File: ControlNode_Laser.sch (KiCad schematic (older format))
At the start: 2 parts

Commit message: Split accels off to separate sheet.
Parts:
- removed P?: CONN_01X07, symbol CONN_01X07
- added C? (x4): 100n, symbol C
- added P?: CONN_01X08_2MNT, symbol CONN_01X08_2MNT
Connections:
- net labels added: LRF_ANALOG_OUT, LRF_RX_232, LRF_TRIGGER_IN, LRF_TRIGGER_OUT, LRF_TX_232
- net labels removed: LRD_Analog_Output, LRD_Trigger_Input, LRF_Rx, LRF_Trigger_Output, LRF_Tx, P1, P2
- wire segments 8 -> 22
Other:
- note added: "Original Author: SafetyLok"
- note added: "rLoop - Control Node"
- note removed: "Test Point x2\n"
- moved on the sheet: U?
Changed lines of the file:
@@
 $Descr A3 16535 11693
 encoding utf-8
-Sheet 2 2
+Sheet 2 3
 Title "Laser Interface"
 Date ""
@@
 Comment4 ""
 $EndDescr
-$Comp
-L CONN_01X07 P?
-U 1 1 5753FF72
-P 4750 3400
-F 0 "P?" H 4750 3800 50  0000 C CNN
-F 1 "CONN_01X07" V 4850 3400 50  0000 C CNN
-F 2 "" H 4750 3400 50  0000 C CNN
-F 3 "" H 4750 3400 50  0000 C CNN
-	1    4750 3400
-	-1   0    0    1
-$EndComp
-Text Notes 4350 2950 0    60   ~ 0
+Text Notes 11700 5200 1    60   ~ 0
 Laser Rangefinder CM3-30\nRS-232
 $Comp
 L +24V #PWR?
 U 1 1 5753FF7A
-P 5350 4000
-F 0 "#PWR?" H 5350 3850 50  0001 C CNN
-F 1 "+24V" H 5350 4140 50  0000 C CNN
-F 2 "" H 5350 4000 50  0000 C CNN
-F 3 "" H 5350 4000 50  0000 C CNN
-	1    5350 4000
+P 10850 4300
+F 0 "#PWR?" H 10850 4150 50  0001 C CNN
+F 1 "+24V" H 10850 4440 50  0000 C CNN
+F 2 "" H 10850 4300 50  0000 C CNN
+F 3 "" H 10850 4300 50  0000 C CNN
+	1    10850 4300
 	1    0    0    -1
 $EndComp
@@
 L GND #PWR?
 U 1 1 5753FF80
-P 5600 3750
-F 0 "#PWR?" H 5600 3500 50  0001 C CNN
-F 1 "GND" H 5600 3600 50  0000 C CNN
-F 2 "" H 5600 3750 50  0000 C CNN
-F 3 "" H 5600 3750 50  0000 C CNN
-	1    5600 3750
+P 10850 4450
+F 0 "#PWR?" H 10850 4200 50  0001 C CNN
+F 1 "GND" H 10850 4300 50  0000 C CNN
+F 2 "" H 10850 4450 50  0000 C CNN
+F 3 "" H 10850 4450 50  0000 C CNN
+	1    10850 4450
+	0    1    1    0
+$EndComp
+$Comp
+L MAX3232 U?
+U 1 1 575400BF
+P 6500 4250
+F 0 "U?" H 7500 4350 60  0000 C CNN
+F 1 "MAX3232" H 7300 2700 60  0000 C CNN
+F 2 "" H 6500 4250 60  0000 C CNN
+F 3 "" H 6500 4250 60  0000 C CNN
+	1    6500 4250
+	1    0    0    -1
+$EndComp
+Text HLabel 5300 5400 0    63   Output ~ 0
+LASER_RX
+Text HLabel 5300 5200 0    63   Input ~ 0
+LASER_TX
+$Comp
+L C C?
+U 1 1 5754B550
+P 5850 4450
+F 0 "C?" H 5875 4550 50  0000 L CNN
+F 1 "100n" H 5875 4350 50  0000 L CNN
+F 2 "" H 5888 4300 50  0000 C CNN
+F 3 "" H 5850 4450 50  0000 C CNN
+	1    5850 4450
+	0    1    1    0
+$EndComp
+$Comp
+L C C?
+U 1 1 5754A89B
+P 5850 4950
+F 0 "C?" H 5875 5050 50  0000 L CNN
+F 1 "100n" H 5875 4850 50  0000 L CNN
+F 2 "" H 5888 4800 50  0000 C CNN
+F 3 "" H 5850 4950 50  0000 C CNN
+	1    5850 4950
+	0    1    1    0
+$EndComp
+$Comp
+L C C?
+U 1 1 5754A977
+P 6650 3900
+F 0 "C?" H 6675 4000 50  0000 L CNN
+F 1 "100n" H 6675 3800 50  0000 L CNN
+F 2 "" H 6688 3750 50  0000 C CNN
+F 3 "" H 6650 3900 50  0000 C CNN
+	1    6650 3900
+	1    0    0    -1
+$EndComp
+$Comp
+L C C?
+U 1 1 5754AA53
+P 6650 6250
+F 0 "C?" H 6675 6350 50  0000 L CNN
+F 1 "100n" H 6675 6150 50  0000 L CNN
+F 2 "" H 6688 6100 50  0000 C CNN
+F 3 "" H 6650 6250 50  0000 C CNN
+	1    6650 6250
 	1    0    0    -1
 $EndComp
 Wire Wire Line
-	4950 3700 4950 4000
+	6000 4450 6300 4450
 Wire Wire Line
-	4950 4000 5350 4000
+	6300 4650 5650 4650
 Wire Wire Line
-	4950 3600 5600 3600
+	5650 4650 5650 4450
 Wire Wire Line
-	5600 3600 5600 3750
+	5650 4450 5700 4450
 Wire Wire Line
-	4950 3500 5600 3500
+	6300 4950 6000 4950
 Wire Wire Line
-	4950 3400 5600 3400
+	6300 4750 5650 4750
 Wire Wire Line
-	4950 3300 6100 3300
+	5650 4750 5650 4950
 Wire Wire Line
-	4950 3200 6100 3200
-Text Label 5250 3500 0    60   ~ 0
-LRF_Tx
-Text Label 5250 3400 0    60   ~ 0
-LRF_Rx
-Text Label 5050 3300 0    60   ~ 0
-LRF_Trigger_Output
-Text Label 5050 3200 0    60   ~ 0
-LRD_Analog_Output
-Text Label 5050 3100 0    60   ~ 0
-LRD_Trigger_Input
-Text Notes 6350 3250 0    60   ~ 0
-Test Point x2\n
-Connection ~ 5600 3200
-Connection ~ 5600 3300
-Text Label 6100 3200 0    60   ~ 0
-P1
-Text Label 6100 3300 0    60   ~ 0
-P2
+	5650 4950 5700 4950
+Wire Wire Line
+	5300 5200 6300 5200
+Wire Wire Line
+	6300 5400 5300 5400
 $Comp
-L MAX3232 U?
-U 1 1 575400BF
-P 8450 3600
-F 0 "U?" H 8550 4300 60  0000 C CNN
-F 1 "MAX3232" H 8550 3150 60  0000 C CNN
-F 2 "" H 8450 3600 60  0000 C CNN
-F 3 "" H 8450 3600 60  0000 C CNN
-	1    8450 3600
+L CONN_01X08_2MNT P?
+U 1 1 5754B07F
+P 11250 4700
+F 0 "P?" H 11250 5150 50  0000 C CNN
+F 1 "CONN_01X08_2MNT" V 11350 4700 50  0000 C CNN
+F 2 "" H 11250 4700 50  0000 C CNN
+F 3 "" H 11250 4700 50  0000 C CNN
+	1    11250 4700
 	1    0    0    -1
 $EndComp
-Text HLabel 11150 3150 0    63   Output ~ 0
-LASER_RX
-Text HLabel 11100 3300 0    63   Input ~ 0
-LASER_TX
+Wire Wire Line
+	11050 4450 10850 4450
+Wire Wire Line
+	11050 4350 10850 4350
+Wire Wire Line
+	10850 4350 10850 4300
+Wire Wire Line
+	7750 5200 8950 5200
+Wire Wire Line
+	8950 5200 8950 4550
+Wire Wire Line
+	8950 4550 11050 4550
+Wire Wire Line
+	7750 5400 9050 5400
+Wire Wire Line
+	9050 5400 9050 4650
+Wire Wire Line
+	9050 4650 11050 4650
+Text Label 9400 4550 0    60   ~ 0
+LRF_TX_232
+Text Label 9400 4650 0    60   ~ 0
+LRF_RX_232
+Wire Wire Line
+	11050 4750 10000 4750
+Wire Wire Line
+	11050 4850 10000 4850
+Wire Wire Line
+	11050 4950 10000 4950
+Text Label 10100 4750 0    60   ~ 0
+LRF_TRIGGER_OUT
+Text Label 10100 4850 0    60   ~ 0
+LRF_ANALOG_OUT
+Text Label 10100 4950 0    60   ~ 0
+LRF_TRIGGER_IN
+Text Notes 11900 10200 0    118  ~ 0
+rLoop - Control Node
+Text Notes 11900 10400 0    60   ~ 0
+Original Author: SafetyLok
 $EndSCHEMATC

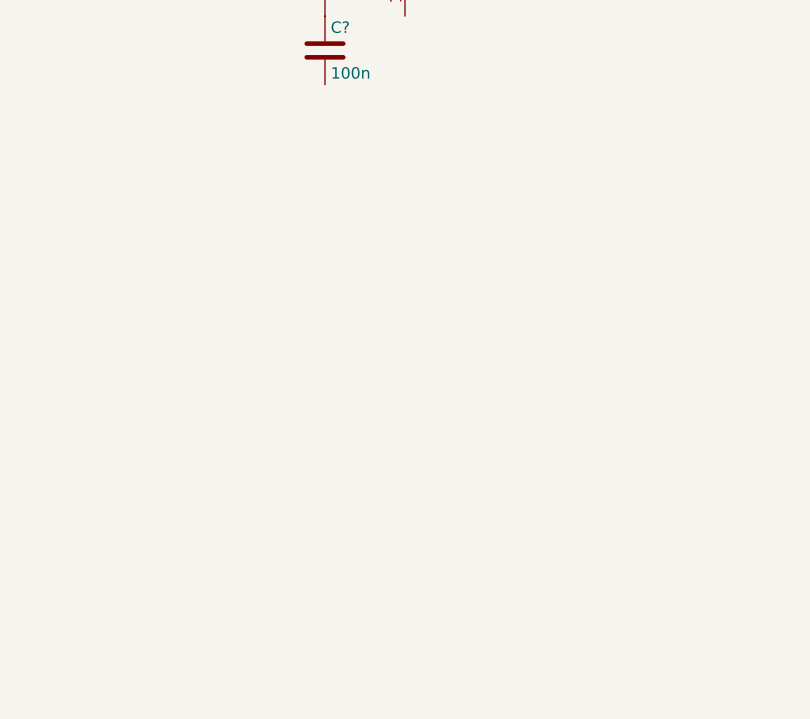
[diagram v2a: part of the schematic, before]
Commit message: Update height sensors.
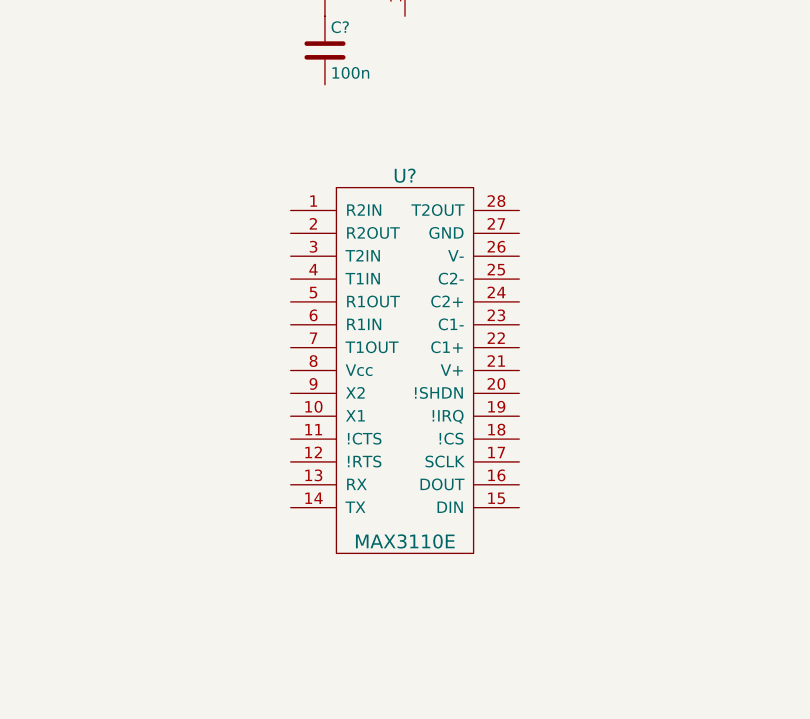
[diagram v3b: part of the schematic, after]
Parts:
- added U?: MAX3110E, symbol MAX3110E-RESCUE-Control_Board
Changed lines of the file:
@@
 Text Notes 11900 10400 0    60   ~ 0
 Original Author: SafetyLok
+$Comp
+L MAX3110E-RESCUE-Control_Board U?
+U 1 1 575676EE
+P 7350 7750
+AR Path="/575676EE" Ref="U?"  Part="1"
+AR Path="/5753FE7B/575676EE" Ref="U?"  Part="1"
+F 0 "U?" H 7000 8700 60  0000 C CNN
+F 1 "MAX3110E" H 7000 7100 60  0000 C CNN
+F 2 "" H 7350 7750 60  0000 C CNN
+F 3 "" H 7350 7750 60  0000 C CNN
+	1    7350 7750
+	1    0    0    -1
+$EndComp
 $EndSCHEMATC

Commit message: Release 1
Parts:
- removed C? (x4): 100n, symbol C
- removed P?: CONN_01X08_2MNT, symbol CONN_01X08_2MNT
- removed U?: MAX3232, symbol MAX3232
- removed U?: MAX3110E, symbol MAX3110E-RESCUE-Control_Board
- added C? (x5): C_100nF_50V, RLOOP_FOOTPRINTS:rLoop_C_0603, symbol C_100nF_50V
- added C? (x2): C_22pF_50V, RLOOP_FOOTPRINTS:rLoop_C_0603, symbol C_22pF_50V
- added P?: TE_640456-8, RLOOP_FOOTPRINTS:rLoop_TE640456-8, symbol TE_640456-8
- added U?: MAX3111EEWI+G36, RLOOP_FOOTPRINTS:rLoop_SOIC28, symbol MAX3111EEWI+G36
- added Y?: MP018S, RLOOP_FOOTPRINTS:rLoop_HC49, symbol MP018S
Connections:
- net labels added: +24V_A, +3V3_A, GNDD, LASER_NCS, LASER_NIRQ, LASER_SPI_MISO, LASER_SPI_MOSI, LASER_SPI_SCK
- net labels removed: +24V, GND, LASER_RX, LASER_TX
- wire segments 22 -> 27
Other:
- note added: "Notes:\n1. All Vreg capacitors are OPTIONAL."

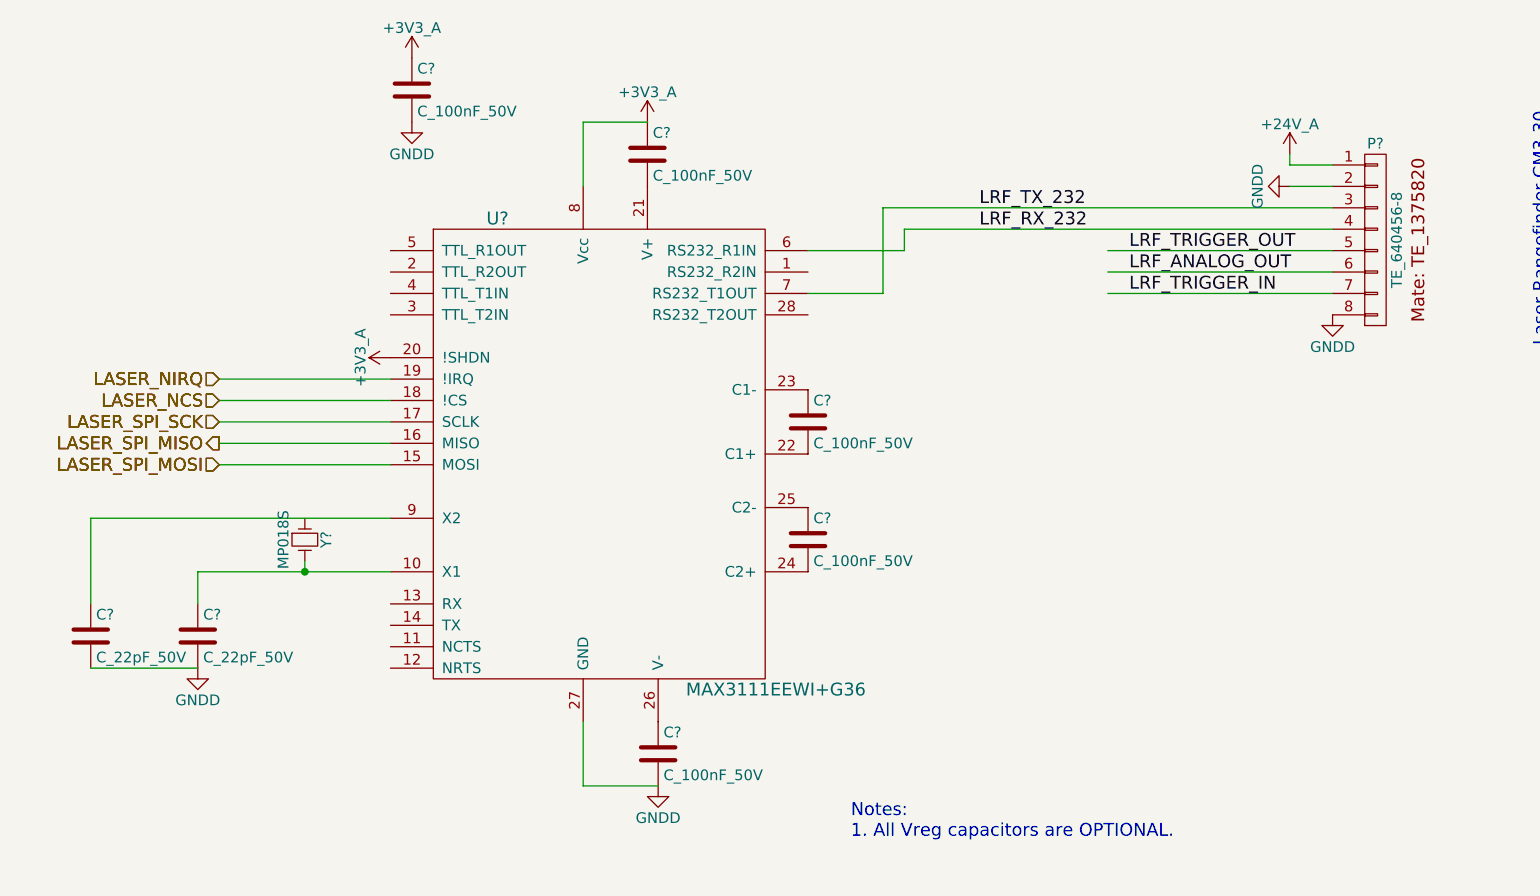
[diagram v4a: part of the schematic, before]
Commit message: Update 10K pullups, 100R on RS422's and additional bypass caps.
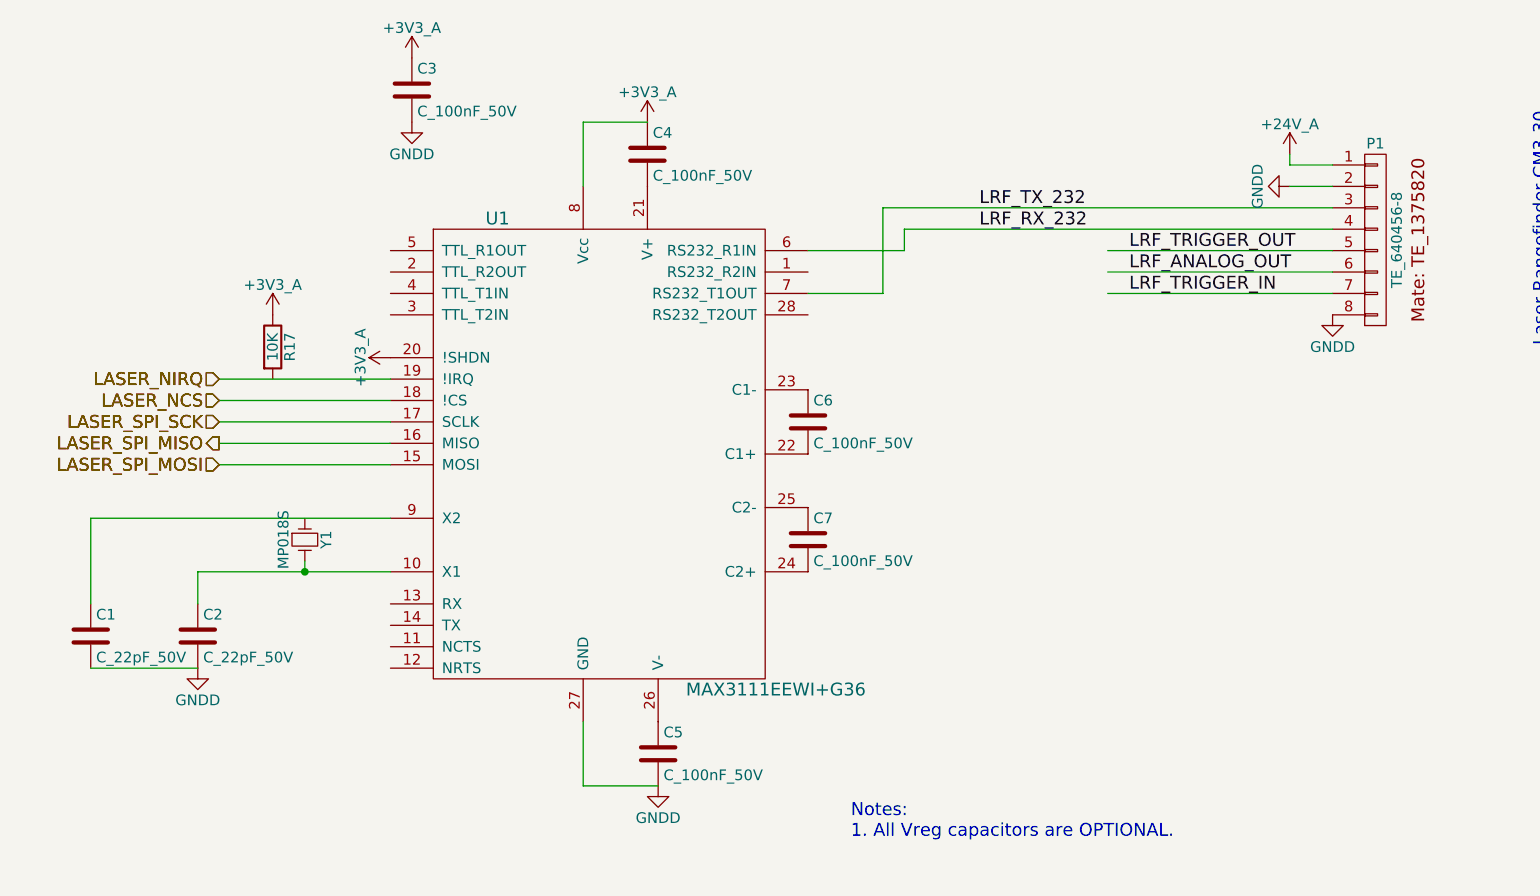
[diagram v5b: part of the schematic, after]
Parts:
- added R17: 10K, RLOOP_FOOTPRINTS:rLoop_R_0603, symbol 10K
- gave numbers to parts that had none: 10
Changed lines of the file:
@@
 Title "Laser Interface"
 Date ""
-Rev "1"
+Rev "2"
 Comp ""
 Comment1 ""
@@
 Original Author: SafetyLok
 $Comp
-L MAX3111EEWI+G36 U?
+L MAX3111EEWI+G36 U1
 U 1 1 575C0EBC
 P 6850 4650
-F 0 "U?" H 7150 4700 60  0000 C CNN
+F 0 "U1" H 7150 4700 60  0000 C CNN
 F 1 "MAX3111EEWI+G36" H 8450 2500 60  0000 C CNN
 F 2 "RLOOP_FOOTPRINTS:rLoop_SOIC28" H 5650 3550 60  0001 C CNN
@@
 $EndComp
 $Comp
-L +3V3_A #PWR?
+L +3V3_A #PWR6
 U 1 1 575C1077
 P 7850 4150
-F 0 "#PWR?" H 7850 4000 50  0001 C CNN
+F 0 "#PWR6" H 7850 4000 50  0001 C CNN
 F 1 "+3V3_A" H 7850 4290 50  0000 C CNN
 F 2 "" H 7850 4150 60  0000 C CNN
@@
 $EndComp
 $Comp
-L C_100nF_50V C?
+L C_100nF_50V C4
 U 1 1 575C108F
 P 7850 4300
-F 0 "C?" H 7875 4400 50  0000 L CNN
+F 0 "C4" H 7875 4400 50  0000 L CNN
 F 1 "C_100nF_50V" H 7875 4200 50  0000 L CNN
 F 2 "RLOOP_FOOTPRINTS:rLoop_C_0603" H 7888 4150 50  0001 C CNN
@@
 $EndComp
 $Comp
-L C_100nF_50V C?
+L C_100nF_50V C6
 U 1 1 575C1108
 P 8600 5550
-F 0 "C?" H 8625 5650 50  0000 L CNN
+F 0 "C6" H 8625 5650 50  0000 L CNN
 F 1 "C_100nF_50V" H 8625 5450 50  0000 L CNN
 F 2 "RLOOP_FOOTPRINTS:rLoop_C_0603" H 8638 5400 50  0001 C CNN
@@
 $EndComp
 $Comp
-L C_100nF_50V C?
+L C_100nF_50V C7
 U 1 1 575C11B8
 P 8600 6100
-F 0 "C?" H 8625 6200 50  0000 L CNN
+F 0 "C7" H 8625 6200 50  0000 L CNN
 F 1 "C_100nF_50V" H 8625 6000 50  0000 L CNN
 F 2 "RLOOP_FOOTPRINTS:rLoop_C_0603" H 8638 5950 50  0001 C CNN
@@
 $EndComp
 $Comp
-L C_100nF_50V C?
+L C_100nF_50V C5
 U 1 1 575C1216
 P 7900 7100
-F 0 "C?" H 7925 7200 50  0000 L CNN
+F 0 "C5" H 7925 7200 50  0000 L CNN
 F 1 "C_100nF_50V" H 7925 7000 50  0000 L CNN
 F 2 "RLOOP_FOOTPRINTS:rLoop_C_0603" H 7938 6950 50  0001 C CNN
@@
 $EndComp
 $Comp
-L GNDD #PWR?
+L GNDD #PWR7
 U 1 1 575C130D
 P 7900 7250
-F 0 "#PWR?" H 7900 7000 50  0001 C CNN
+F 0 "#PWR7" H 7900 7000 50  0001 C CNN
 F 1 "GNDD" H 7900 7100 50  0000 C CNN
 F 2 "" H 7900 7250 50  0000 C CNN
@@
 	8950 4950 8600 4950
 $Comp
-L +3V3_A #PWR?
+L +3V3_A #PWR3
 U 1 1 575C19C3
 P 6650 5250
-F 0 "#PWR?" H 6650 5100 50  0001 C CNN
+F 0 "#PWR3" H 6650 5100 50  0001 C CNN
 F 1 "+3V3_A" H 6650 5390 50  0000 C CNN
 F 2 "" H 6650 5250 60  0000 C CNN
@@
 LASER_SPI_MOSI
 $Comp
-L TE_640456-8 P?
+L TE_640456-8 P1
 U 1 1 575C1CCE
 P 11200 4300
-F 0 "P?" H 11250 4350 50  0000 C CNN
+F 0 "P1" H 11250 4350 50  0000 C CNN
 F 1 "TE_640456-8" V 11350 3900 50  0000 C CNN
 F 2 "RLOOP_FOOTPRINTS:rLoop_TE640456-8" H 11250 3900 50  0001 C CNN
@@
 $EndComp
 $Comp
-L +24V_A #PWR?
+L +24V_A #PWR8
 U 1 1 575C1E6C
 P 10850 4300
-F 0 "#PWR?" H 10850 4150 50  0001 C CNN
+F 0 "#PWR8" H 10850 4150 50  0001 C CNN
 F 1 "+24V_A" H 10850 4440 50  0000 C CNN
 F 2 "" H 10850 4300 60  0000 C CNN
@@
 $EndComp
 $Comp
-L GNDD #PWR?
+L GNDD #PWR10
 U 1 1 575C1E8C
 P 11050 5050
-F 0 "#PWR?" H 11050 4800 50  0001 C CNN
+F 0 "#PWR10" H 11050 4800 50  0001 C CNN
 F 1 "GNDD" H 11050 4900 50  0000 C CNN
 F 2 "" H 11050 5050 50  0000 C CNN
@@
 $EndComp
 $Comp
-L GNDD #PWR?
+L GNDD #PWR9
 U 1 1 575C1EB0
 P 10850 4450
-F 0 "#PWR?" H 10850 4200 50  0001 C CNN
+F 0 "#PWR9" H 10850 4200 50  0001 C CNN
 F 1 "GNDD" H 10850 4300 50  0000 C CNN
 F 2 "" H 10850 4450 50  0000 C CNN
@@
 Notes:\n1. All Vreg capacitors are OPTIONAL.
 $Comp
-L MP018S Y?
+L MP018S Y1
 U 1 1 575C89BF
 P 6250 6100
-F 0 "Y?" H 6250 6200 50  0000 C CNN
+F 0 "Y1" H 6250 6200 50  0000 C CNN
 F 1 "MP018S" H 6250 6000 50  0000 C CNN
 F 2 "RLOOP_FOOTPRINTS:rLoop_HC49" H 6150 6100 50  0001 C CNN
@@
 $EndComp
 $Comp
-L C_22pF_50V C?
+L C_22pF_50V C2
 U 1 1 575C8DFE
 P 5750 6550
-F 0 "C?" H 5775 6650 50  0000 L CNN
+F 0 "C2" H 5775 6650 50  0000 L CNN
 F 1 "C_22pF_50V" H 5775 6450 50  0000 L CNN
 F 2 "RLOOP_FOOTPRINTS:rLoop_C_0603" H 5788 6400 50  0001 C CNN
@@
 $EndComp
 $Comp
-L C_22pF_50V C?
+L C_22pF_50V C1
 U 1 1 575C8E57
 P 5250 6550
-F 0 "C?" H 5275 6650 50  0000 L CNN
+F 0 "C1" H 5275 6650 50  0000 L CNN
 F 1 "C_22pF_50V" H 5275 6450 50  0000 L CNN
 F 2 "RLOOP_FOOTPRINTS:rLoop_C_0603" H 5288 6400 50  0001 C CNN
@@
 	5250 6700 5750 6700
 $Comp
-L GNDD #PWR?
+L GNDD #PWR1
 U 1 1 575C8F20
 P 5750 6700
-F 0 "#PWR?" H 5750 6450 50  0001 C CNN
+F 0 "#PWR1" H 5750 6450 50  0001 C CNN
 F 1 "GNDD" H 5750 6550 50  0000 C CNN
 F 2 "" H 5750 6700 50  0000 C CNN
@@
 $EndComp
 $Comp
-L C_100nF_50V C?
+L C_100nF_50V C3
 U 1 1 575C92AE
 P 6750 4000
-F 0 "C?" H 6775 4100 50  0000 L CNN
+F 0 "C3" H 6775 4100 50  0000 L CNN
 F 1 "C_100nF_50V" H 6775 3900 50  0000 L CNN
 F 2 "RLOOP_FOOTPRINTS:rLoop_C_0603" H 6788 3850 50  0001 C CNN
@@
 $EndComp
 $Comp
-L +3V3_A #PWR?
+L +3V3_A #PWR4
 U 1 1 575C92C0
 P 6750 3850
-F 0 "#PWR?" H 6750 3700 50  0001 C CNN
+F 0 "#PWR4" H 6750 3700 50  0001 C CNN
 F 1 "+3V3_A" H 6750 3990 50  0000 C CNN
 F 2 "" H 6750 3850 60  0000 C CNN
@@
 $EndComp
 $Comp
-L GNDD #PWR?
+L GNDD #PWR5
 U 1 1 575C92D4
 P 6750 4150
-F 0 "#PWR?" H 6750 3900 50  0001 C CNN
+F 0 "#PWR5" H 6750 3900 50  0001 C CNN
 F 1 "GNDD" H 6750 4000 50  0000 C CNN
 F 2 "" H 6750 4150 50  0000 C CNN
@@
 	1    0    0    -1
 $EndComp
+$Comp
+L 10K R17
+U 1 1 575CD679
+P 6100 5200
+F 0 "R17" V 6180 5200 50  0000 C CNN
+F 1 "10K" V 6100 5200 50  0000 C CNN
+F 2 "RLOOP_FOOTPRINTS:rLoop_R_0603" V 6030 5200 50  0001 C CNN
+F 3 "" H 6100 5200 50  0000 C CNN
+	1    6100 5200
+	1    0    0    -1
+$EndComp
+$Comp
+L +3V3_A #PWR2
+U 1 1 575CD6CC
+P 6100 5050
+F 0 "#PWR2" H 6100 4900 50  0001 C CNN
+F 1 "+3V3_A" H 6100 5190 50  0000 C CNN
+F 2 "" H 6100 5050 60  0000 C CNN
+F 3 "" H 6100 5050 60  0000 C CNN
+	1    6100 5050
+	1    0    0    -1
+$EndComp
